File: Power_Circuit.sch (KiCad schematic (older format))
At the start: 33 parts, among them U1 B_Plug_5mm, U10 DSN2596, U11 B_Plug_5mm, U12 B_Plug_5mm, U13 B_Plug_5mm, U2 DSN2596, U3 DSN2596, U4 B_Plug_5mm, U5 B_Plug_5mm, U6 B_Plug_5mm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

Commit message: Nouvelle avancee, manque la protection reverse polarity
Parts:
- removed C1: CP, symbol Device:CP
- removed D1: LED, symbol Device:LED
- removed D2: D, symbol Device:D
- removed F1: Fuse, symbol Device:Fuse
- removed R1: R, symbol Device:R
- added BZ1: Buzzer, Buzzer_Beeper:Buzzer_12x9.5RM7.6, symbol Device:Buzzer
- added J1: Conn_01x09, symbol Connector_Generic:Conn_01x09
- added J2: Conn_01x04, symbol Connector_Generic:Conn_01x04
- added SW1: SW_Push, symbol Switch:SW_Push
- D3, D4, D5, D6, D7: footprint (none) -> LIB_BE_PHELMA_CMS:LED_1206_3216Metric_Pad1.42x1.75mm_HandSolder
- R2, R3, R4, R5, R6: footprint (none) -> LIB_BE_PHELMA_CMS:R_1206_3216Metric_Pad1.42x1.75mm_HandSolder
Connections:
- wire segments 100 -> 114
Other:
- note added: "Battery balance connector"
- note added: "Battery bipper buzzer"
- note added: "Battery bipper slot"
- note added: "Bipper\n"
- note added: "Reset if battery went too low"
- note removed: "Add a slot for a battery bipper"
- moved on the sheet: U1

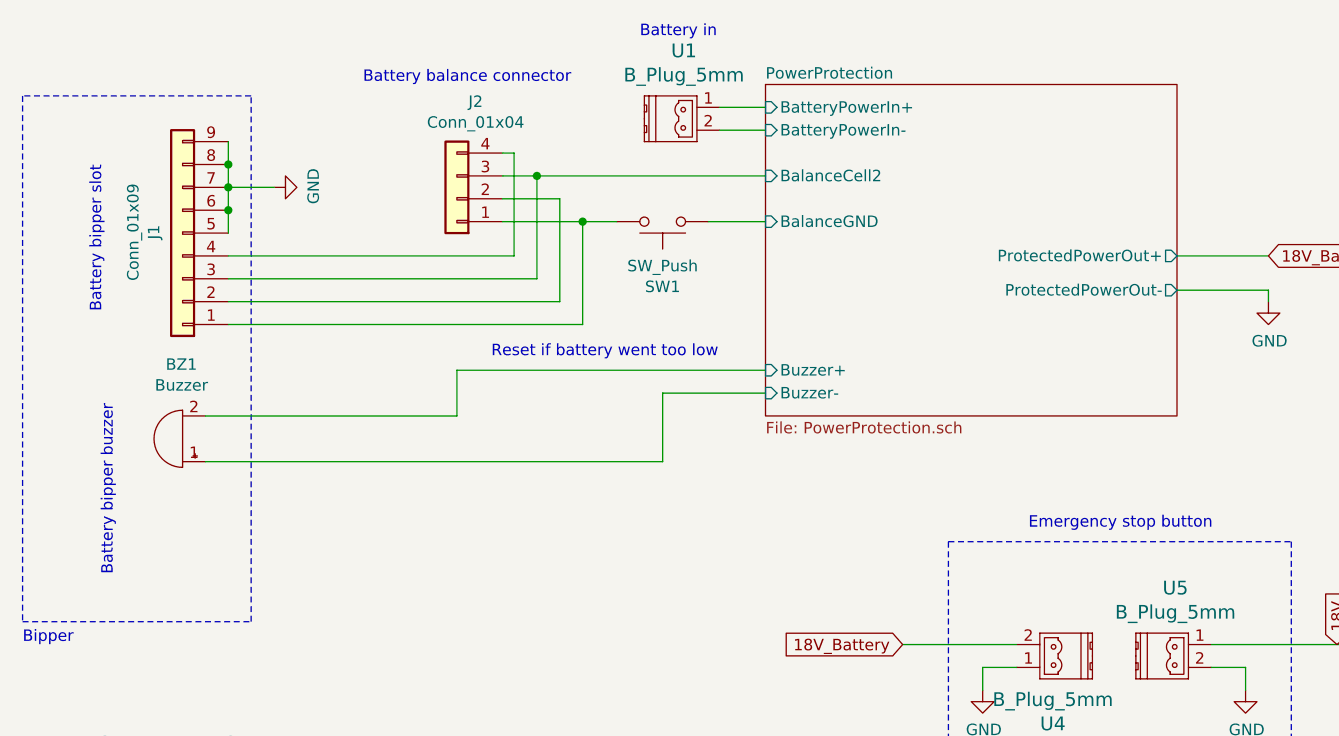
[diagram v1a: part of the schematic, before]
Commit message: Il reste a trouver empreintes et router
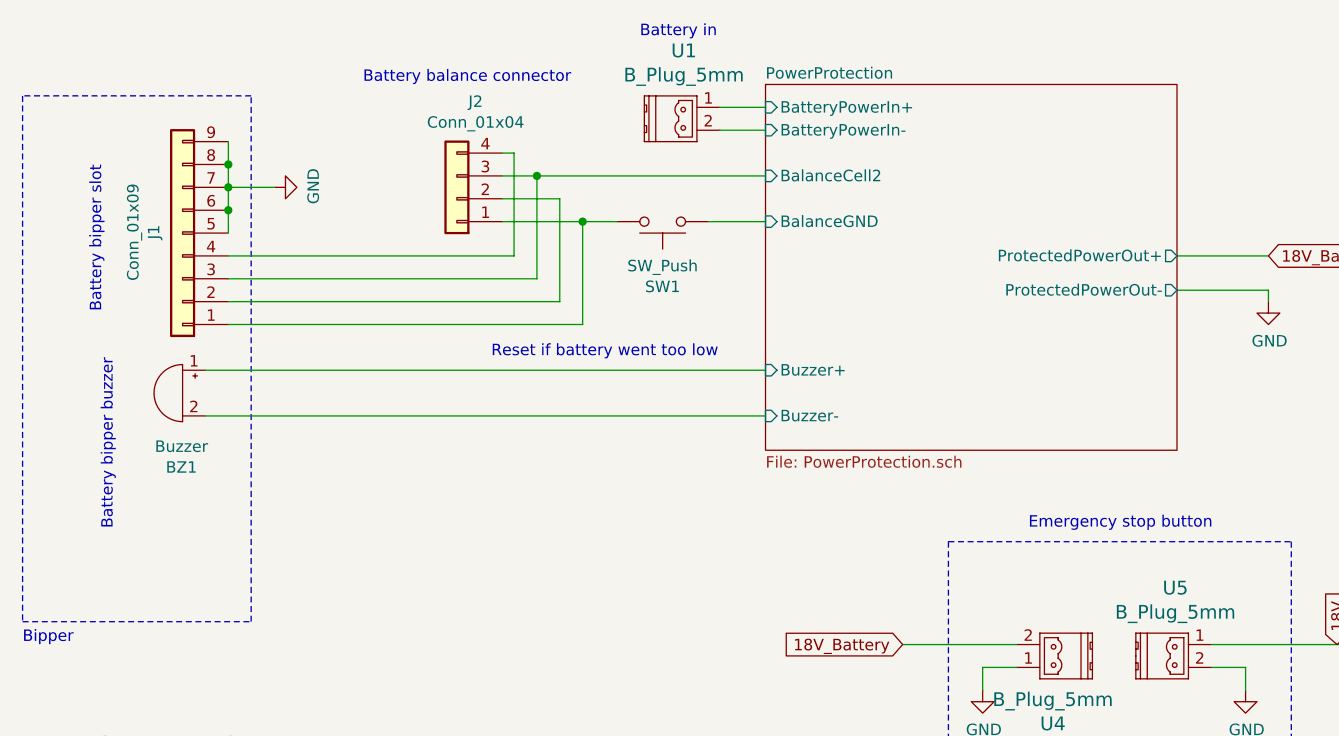
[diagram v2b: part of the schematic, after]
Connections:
- net PowerProtection/Buzzer+: now also BZ1.1 (-); no longer BZ1.2 (+)
- net PowerProtection/Buzzer-: now also BZ1.2 (+); no longer BZ1.1 (-)
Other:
- moved on the sheet: BZ1
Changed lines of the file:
@@
 $Descr A4 11693 8268
 encoding utf-8
-Sheet 1 3
+Sheet 1 2
 Title ""
 Date ""
@@
 Connection ~ 3350 5500
 $Sheet
-S 4250 1050 1800 1450
+S 4250 1050 1800 1600
 U 5F802FB9
 F0 "PowerProtection" 50
@@
 F7 "BalanceCell2" I L 4250 1450 50
 F8 "Buzzer+" I L 4250 2300 50
-F9 "Buzzer-" I L 4250 2400 50
+F9 "Buzzer-" I L 4250 2500 50
 $EndSheet
 Wire Wire Line
@@
 Wire Wire Line
 	3100 1550 3350 1550
-Text Notes 1400 3200 1    50   ~ 0
+Text Notes 1400 3000 1    50   ~ 0
 Battery bipper buzzer
 $Comp
 L Device:Buzzer BZ1
 U 1 1 5F94563A
-P 1700 2600
-F 0 "BZ1" H 1705 2275 50  0000 C CNN
-F 1 "Buzzer" H 1705 2366 50  0000 C CNN
-F 2 "Buzzer_Beeper:Buzzer_12x9.5RM7.6" V 1675 2700 50  0001 C CNN
-F 3 "~" V 1675 2700 50  0001 C CNN
-	1    1700 2600
-	-1   0    0    1
+P 1700 2400
+F 0 "BZ1" H 1705 2075 50  0000 C CNN
+F 1 "Buzzer" H 1705 2166 50  0000 C CNN
+F 2 "Buzzer_Beeper:Buzzer_12x9.5RM7.6" V 1675 2500 50  0001 C CNN
+F 3 "~" V 1675 2500 50  0001 C CNN
+	1    1700 2400
+	-1   0    0    -1
 $EndComp
 Wire Wire Line
@@
 Wire Wire Line
 	3450 1650 3100 1650
-Wire Wire Line
-	4250 2300 2900 2300
-Wire Wire Line
-	2900 2300 2900 2500
-Wire Wire Line
-	2900 2500 1800 2500
 Wire Wire Line
 	1900 1300 1900 1400
@@
 	-1   0    0    1
 $EndComp
-Wire Wire Line
-	3800 2700 3800 2400
-Wire Wire Line
-	3800 2400 4250 2400
 Text Notes 3050 2250 0    50   ~ 0
 Reset if battery went too low
@@
 Connection ~ 3450 1650
 Wire Wire Line
-	1800 2700 3800 2700
-Wire Wire Line
 	10200 3000 10250 3000
 Wire Wire Line
@@
 Wire Wire Line
 	1750 4100 1750 4200
+Wire Wire Line
+	1800 2300 4250 2300
+Wire Wire Line
+	1800 2500 4250 2500
 $EndSCHEMATC

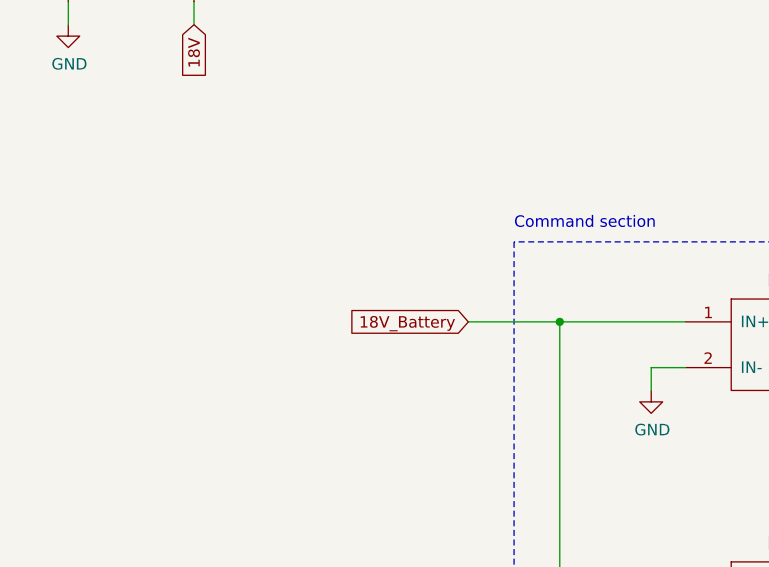
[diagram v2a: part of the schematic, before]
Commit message: ajout de la tirette
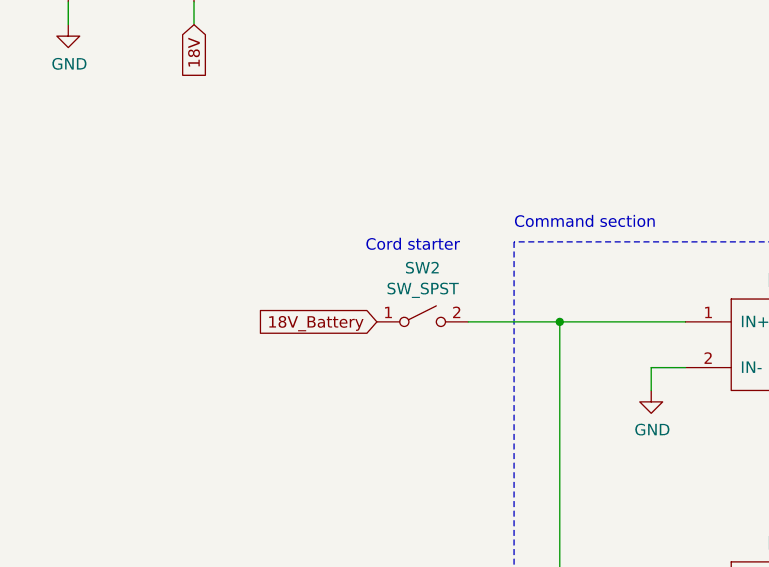
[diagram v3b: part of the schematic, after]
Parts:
- added SW2: SW_SPST, symbol Switch:SW_SPST
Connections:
- net 18V_Battery: now also SW2.1 (A); no longer U2.1 (IN+), U3.1 (IN+)
- new net: SW2.2 (B), U2.1 (IN+), U3.1 (IN+)
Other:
- note added: "Cord starter"
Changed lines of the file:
@@
 encoding utf-8
 Sheet 1 2
-Title ""
+Title "Power Circuit"
 Date ""
 Rev ""
-Comp ""
+Comp "Robotronik"
 Comment1 ""
 Comment2 ""
@@
 Text GLabel 4850 3500 0    50   Input ~ 0
 18V_Battery
-Text GLabel 2950 5500 0    50   Input ~ 0
+Text GLabel 2550 5500 0    50   Input ~ 0
 18V_Battery
 Wire Wire Line
@@
 Wire Wire Line
 	1800 2500 4250 2500
+$Comp
+L Switch:SW_SPST SW2
+U 1 1 5F8A3132
+P 2750 5500
+F 0 "SW2" H 2750 5735 50  0000 C CNN
+F 1 "SW_SPST" H 2750 5644 50  0000 C CNN
+F 2 "" H 2750 5500 50  0001 C CNN
+F 3 "~" H 2750 5500 50  0001 C CNN
+	1    2750 5500
+	1    0    0    -1
+$EndComp
+Text Notes 2500 5200 0    50   ~ 0
+Cord starter
 $EndSCHEMATC

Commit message: Fin du schema et routage
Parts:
- added BZ2: Buzzer, Buzzer_Beeper:Buzzer_12x9.5RM7.6, symbol Device:Buzzer
- F2, F3, F4, F5, F6: footprint (none) -> Fuse:Fuse_1210_3225Metric_Pad1.42x2.65mm_HandSolder
- J1: footprint (none) -> Connector_PinSocket_2.54mm:PinSocket_1x09_P2.54mm_Horizontal
- J2: footprint (none) -> Connector_PinHeader_2.54mm:PinHeader_1x04_P2.54mm_Vertical
- SW1: footprint (none) -> LIB_BE_PHELMA:R_Axial_DIN0207_L6.3mm_D2.5mm_P10.16mm_Horizontal
- SW2: value SW_SPST -> SW_STARTER; footprint (none) -> LIB_BE_PHELMA:R_Axial_DIN0207_L6.3mm_D2.5mm_P10.16mm_Horizontal
- U1: value B_Plug_5mm -> B_Plug_Battery_In; footprint (none) -> Connector_Phoenix_MC:PhoenixContact_MCV_1,5_2-G-3.81_1x02_P3.81mm_Vertical
- U10, U2, U3, U8, U9: footprint (none) -> DC_DC_LM2596_small:DC_DC_LM2596_small
- U11: value B_Plug_5mm -> B_Plug_12v_Motor1; footprint (none) -> Connector_Phoenix_MC:PhoenixContact_MCV_1,5_2-G-3.81_1x02_P3.81mm_Vertical
- U12: value B_Plug_5mm -> B_Plug_12v_Motor2; footprint (none) -> Connector_Phoenix_MC:PhoenixContact_MCV_1,5_2-G-3.81_1x02_P3.81mm_Vertical
- U13: value B_Plug_5mm -> B_Plug_5v_Actuator; footprint (none) -> Connector_Phoenix_MC:PhoenixContact_MCV_1,5_2-G-3.81_1x02_P3.81mm_Vertical
- U4: value B_Plug_5mm -> B_Plug_E-Stop_In; footprint (none) -> Connector_Phoenix_MC:PhoenixContact_MCV_1,5_2-G-3.81_1x02_P3.81mm_Vertical
- U5: value B_Plug_5mm -> B_Plug_E-Stop_out; footprint (none) -> Connector_Phoenix_MC:PhoenixContact_MCV_1,5_2-G-3.81_1x02_P3.81mm_Vertical
- U6: value B_Plug_5mm -> B_Plug_5V_Command; footprint (none) -> Connector_Phoenix_MC:PhoenixContact_MCV_1,5_2-G-3.81_1x02_P3.81mm_Vertical
- U7: value B_Plug_5mm -> B_Plug_7v5_Command; footprint (none) -> Connector_Phoenix_MC:PhoenixContact_MCV_1,5_2-G-3.81_1x02_P3.81mm_Vertical
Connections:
- net 18V: now also U5.2; no longer U5.1
- net GND: now also U5.1, BZ2.1 (-), BZ2.2 (+); no longer U5.2
- net PowerProtection/BatteryPowerIn+: now also U1.2; no longer U1.1
- net PowerProtection/BatteryPowerIn-: now also U1.1; no longer U1.2
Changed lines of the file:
@@
 F 0 "U8" H 8500 3587 60  0000 C CNN
 F 1 "DSN2596" H 8500 3481 60  0000 C CNN
-F 2 "" H 8500 3200 60  0001 C CNN
+F 2 "DC_DC_LM2596_small:DC_DC_LM2596_small" H 8500 3200 60  0001 C CNN
 F 3 "" H 8500 3200 60  0000 C CNN
 	1    8500 3200
@@
 F 0 "F4" H 9460 3146 50  0000 L CNN
 F 1 "Fuse" H 9460 3055 50  0000 L CNN
-F 2 "" V 9330 3100 50  0001 C CNN
+F 2 "Fuse:Fuse_1210_3225Metric_Pad1.42x2.65mm_HandSolder" V 9330 3100 50  0001 C CNN
 F 3 "~" H 9400 3100 50  0001 C CNN
 	1    9400 3100
@@
 P 3950 1200
 F 0 "U1" H 3893 1497 60  0000 C CNN
-F 1 "B_Plug_5mm" H 3893 1391 60  0000 C CNN
-F 2 "" H 3950 1200 60  0001 C CNN
+F 1 "B_Plug_Battery_In" H 3893 1391 60  0000 C CNN
+F 2 "Connector_Phoenix_MC:PhoenixContact_MCV_1,5_2-G-3.81_1x02_P3.81mm_Vertical" H 3950 1200 60  0001 C CNN
 F 3 "" H 3950 1200 60  0000 C CNN
 	1    3950 1200
-	1    0    0    -1
+	1    0    0    1
 $EndComp
 $Comp
@@
 P 10500 3150
 F 0 "U11" H 10443 3447 60  0000 C CNN
-F 1 "B_Plug_5mm" H 10443 3341 60  0000 C CNN
-F 2 "" H 10500 3150 60  0001 C CNN
+F 1 "B_Plug_12v_Motor1" H 10443 3341 60  0000 C CNN
+F 2 "Connector_Phoenix_MC:PhoenixContact_MCV_1,5_2-G-3.81_1x02_P3.81mm_Vertical" H 10500 3150 60  0001 C CNN
 F 3 "" H 10500 3150 60  0000 C CNN
 	1    10500 3150
@@
 F 0 "U9" H 8500 4687 60  0000 C CNN
 F 1 "DSN2596" H 8500 4581 60  0000 C CNN
-F 2 "" H 8500 4300 60  0001 C CNN
+F 2 "DC_DC_LM2596_small:DC_DC_LM2596_small" H 8500 4300 60  0001 C CNN
 F 3 "" H 8500 4300 60  0000 C CNN
 	1    8500 4300
@@
 F 0 "F5" H 9460 4246 50  0000 L CNN
 F 1 "Fuse" H 9460 4155 50  0000 L CNN
-F 2 "" V 9330 4200 50  0001 C CNN
+F 2 "Fuse:Fuse_1210_3225Metric_Pad1.42x2.65mm_HandSolder" V 9330 4200 50  0001 C CNN
 F 3 "~" H 9400 4200 50  0001 C CNN
 	1    9400 4200
@@
 P 10500 4250
 F 0 "U12" H 10443 4547 60  0000 C CNN
-F 1 "B_Plug_5mm" H 10443 4441 60  0000 C CNN
-F 2 "" H 10500 4250 60  0001 C CNN
+F 1 "B_Plug_12v_Motor2" H 10443 4441 60  0000 C CNN
+F 2 "Connector_Phoenix_MC:PhoenixContact_MCV_1,5_2-G-3.81_1x02_P3.81mm_Vertical" H 10500 4250 60  0001 C CNN
 F 3 "" H 10500 4250 60  0000 C CNN
 	1    10500 4250
@@
 F 0 "U10" H 8500 5787 60  0000 C CNN
 F 1 "DSN2596" H 8500 5681 60  0000 C CNN
-F 2 "" H 8500 5400 60  0001 C CNN
+F 2 "DC_DC_LM2596_small:DC_DC_LM2596_small" H 8500 5400 60  0001 C CNN
 F 3 "" H 8500 5400 60  0000 C CNN
 	1    8500 5400
@@
 F 0 "F6" H 9460 5346 50  0000 L CNN
 F 1 "Fuse" H 9460 5255 50  0000 L CNN
-F 2 "" V 9330 5300 50  0001 C CNN
+F 2 "Fuse:Fuse_1210_3225Metric_Pad1.42x2.65mm_HandSolder" V 9330 5300 50  0001 C CNN
 F 3 "~" H 9400 5300 50  0001 C CNN
 	1    9400 5300
@@
 P 10500 5350
 F 0 "U13" H 10443 5647 60  0000 C CNN
-F 1 "B_Plug_5mm" H 10443 5541 60  0000 C CNN
-F 2 "" H 10500 5350 60  0001 C CNN
+F 1 "B_Plug_5v_Actuator" H 10443 5541 60  0000 C CNN
+F 2 "Connector_Phoenix_MC:PhoenixContact_MCV_1,5_2-G-3.81_1x02_P3.81mm_Vertical" H 10500 5350 60  0001 C CNN
 F 3 "" H 10500 5350 60  0000 C CNN
 	1    10500 5350
@@
 F 0 "U2" H 4450 5987 60  0000 C CNN
 F 1 "DSN2596" H 4450 5881 60  0000 C CNN
-F 2 "" H 4450 5600 60  0001 C CNN
+F 2 "DC_DC_LM2596_small:DC_DC_LM2596_small" H 4450 5600 60  0001 C CNN
 F 3 "https://www.ti.com/lit/ds/symlink/lm2596.pdf" H 4450 5600 60  0001 C CNN
 	1    4450 5600
@@
 F 0 "F2" H 5410 5546 50  0000 L CNN
 F 1 "Fuse" H 5410 5455 50  0000 L CNN
-F 2 "" V 5280 5500 50  0001 C CNN
+F 2 "Fuse:Fuse_1210_3225Metric_Pad1.42x2.65mm_HandSolder" V 5280 5500 50  0001 C CNN
 F 3 "~" H 5350 5500 50  0001 C CNN
 	1    5350 5500
@@
 P 6450 5550
 F 0 "U6" H 6393 5847 60  0000 C CNN
-F 1 "B_Plug_5mm" H 6393 5741 60  0000 C CNN
-F 2 "" H 6450 5550 60  0001 C CNN
+F 1 "B_Plug_5V_Command" H 6393 5741 60  0000 C CNN
+F 2 "Connector_Phoenix_MC:PhoenixContact_MCV_1,5_2-G-3.81_1x02_P3.81mm_Vertical" H 6450 5550 60  0001 C CNN
 F 3 "" H 6450 5550 60  0000 C CNN
 	1    6450 5550
@@
 F 0 "U3" H 4450 7137 60  0000 C CNN
 F 1 "DSN2596" H 4450 7031 60  0000 C CNN
-F 2 "" H 4450 6750 60  0001 C CNN
+F 2 "DC_DC_LM2596_small:DC_DC_LM2596_small" H 4450 6750 60  0001 C CNN
 F 3 "" H 4450 6750 60  0000 C CNN
 	1    4450 6750
@@
 F 0 "F3" H 5410 6696 50  0000 L CNN
 F 1 "Fuse" H 5410 6605 50  0000 L CNN
-F 2 "" V 5280 6650 50  0001 C CNN
+F 2 "Fuse:Fuse_1210_3225Metric_Pad1.42x2.65mm_HandSolder" V 5280 6650 50  0001 C CNN
 F 3 "~" H 5350 6650 50  0001 C CNN
 	1    5350 6650
@@
 P 6450 6700
 F 0 "U7" H 6393 6997 60  0000 C CNN
-F 1 "B_Plug_5mm" H 6393 6891 60  0000 C CNN
-F 2 "" H 6450 6700 60  0001 C CNN
+F 1 "B_Plug_7v5_Command" H 6393 6891 60  0000 C CNN
+F 2 "Connector_Phoenix_MC:PhoenixContact_MCV_1,5_2-G-3.81_1x02_P3.81mm_Vertical" H 6450 6700 60  0001 C CNN
 F 3 "" H 6450 6700 60  0000 C CNN
 	1    6450 6700
@@
 P 5450 3550
 F 0 "U4" H 5393 3847 60  0000 C CNN
-F 1 "B_Plug_5mm" H 5393 3741 60  0000 C CNN
-F 2 "" H 5450 3550 60  0001 C CNN
+F 1 "B_Plug_E-Stop_In" H 5393 3741 60  0000 C CNN
+F 2 "Connector_Phoenix_MC:PhoenixContact_MCV_1,5_2-G-3.81_1x02_P3.81mm_Vertical" H 5450 3550 60  0001 C CNN
 F 3 "" H 5450 3550 60  0000 C CNN
 	1    5450 3550
@@
 P 6100 3550
 F 0 "U5" H 6043 3847 60  0000 C CNN
-F 1 "B_Plug_5mm" H 6043 3741 60  0000 C CNN
-F 2 "" H 6100 3550 60  0001 C CNN
+F 1 "B_Plug_E-Stop_out" H 6043 3741 60  0000 C CNN
+F 2 "Connector_Phoenix_MC:PhoenixContact_MCV_1,5_2-G-3.81_1x02_P3.81mm_Vertical" H 6100 3550 60  0001 C CNN
 F 3 "" H 6100 3550 60  0000 C CNN
 	1    6100 3550
-	1    0    0    -1
+	1    0    0    1
 $EndComp
 Wire Wire Line
@@
 F 0 "J1" V 1825 1696 50  0000 C CNN
 F 1 "Conn_01x09" V 1916 1696 50  0000 C CNN
-F 2 "" H 1700 1700 50  0001 C CNN
+F 2 "Connector_PinSocket_2.54mm:PinSocket_1x09_P2.54mm_Horizontal" H 1700 1700 50  0001 C CNN
 F 3 "~" H 1700 1700 50  0001 C CNN
 	1    1700 1700
@@
 F 0 "J2" H 2818 1125 50  0000 C CNN
 F 1 "Conn_01x04" H 2818 1216 50  0000 C CNN
-F 2 "" H 2900 1550 50  0001 C CNN
+F 2 "Connector_PinHeader_2.54mm:PinHeader_1x04_P2.54mm_Vertical" H 2900 1550 50  0001 C CNN
 F 3 "~" H 2900 1550 50  0001 C CNN
 	1    2900 1550
@@
 F 0 "SW1" H 3800 1935 50  0000 C CNN
 F 1 "SW_Push" H 3800 1844 50  0000 C CNN
-F 2 "" H 3800 1850 50  0001 C CNN
+F 2 "LIB_BE_PHELMA:R_Axial_DIN0207_L6.3mm_D2.5mm_P10.16mm_Horizontal" H 3800 1850 50  0001 C CNN
 F 3 "~" H 3800 1850 50  0001 C CNN
 	1    3800 1650
@@
 P 2750 5500
 F 0 "SW2" H 2750 5735 50  0000 C CNN
-F 1 "SW_SPST" H 2750 5644 50  0000 C CNN
-F 2 "" H 2750 5500 50  0001 C CNN
+F 1 "SW_STARTER" H 2750 5644 50  0000 C CNN
+F 2 "LIB_BE_PHELMA:R_Axial_DIN0207_L6.3mm_D2.5mm_P10.16mm_Horizontal" H 2750 5500 50  0001 C CNN
 F 3 "~" H 2750 5500 50  0001 C CNN
 	1    2750 5500
@@
 Text Notes 2500 5200 0    50   ~ 0
 Cord starter
+$Comp
+L Device:Buzzer BZ2
+U 1 1 5FB3C6D2
+P 1750 2950
+F 0 "BZ2" H 1755 2625 50  0000 C CNN
+F 1 "Buzzer" H 1755 2716 50  0000 C CNN
+F 2 "Buzzer_Beeper:Buzzer_12x9.5RM7.6" V 1725 3050 50  0001 C CNN
+F 3 "~" V 1725 3050 50  0001 C CNN
+	1    1750 2950
+	-1   0    0    -1
+$EndComp
+$Comp
+L power:GND #PWR0102
+U 1 1 5FB60BCF
+P 2050 2850
+F 0 "#PWR0102" H 2050 2600 50  0001 C CNN
+F 1 "GND" H 2055 2677 50  0000 C CNN
+F 2 "" H 2050 2850 50  0001 C CNN
+F 3 "" H 2050 2850 50  0001 C CNN
+	1    2050 2850
+	0    -1   -1   0
+$EndComp
+Wire Wire Line
+	2050 2850 1850 2850
+$Comp
+L power:GND #PWR0103
+U 1 1 5FB650C4
+P 2050 3050
+F 0 "#PWR0103" H 2050 2800 50  0001 C CNN
+F 1 "GND" H 2055 2877 50  0000 C CNN
+F 2 "" H 2050 3050 50  0001 C CNN
+F 3 "" H 2050 3050 50  0001 C CNN
+	1    2050 3050
+	0    -1   -1   0
+$EndComp
+Wire Wire Line
+	2050 3050 1850 3050
 $EndSCHEMATC

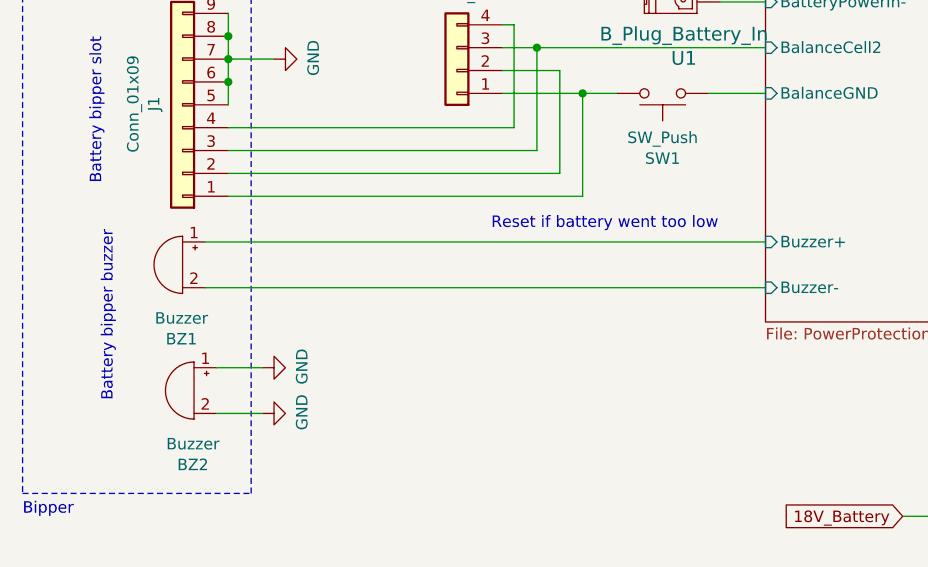
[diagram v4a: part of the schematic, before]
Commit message: Changement pour ajouter la possibiliter de court circuiter les 2 buzzers ou 1
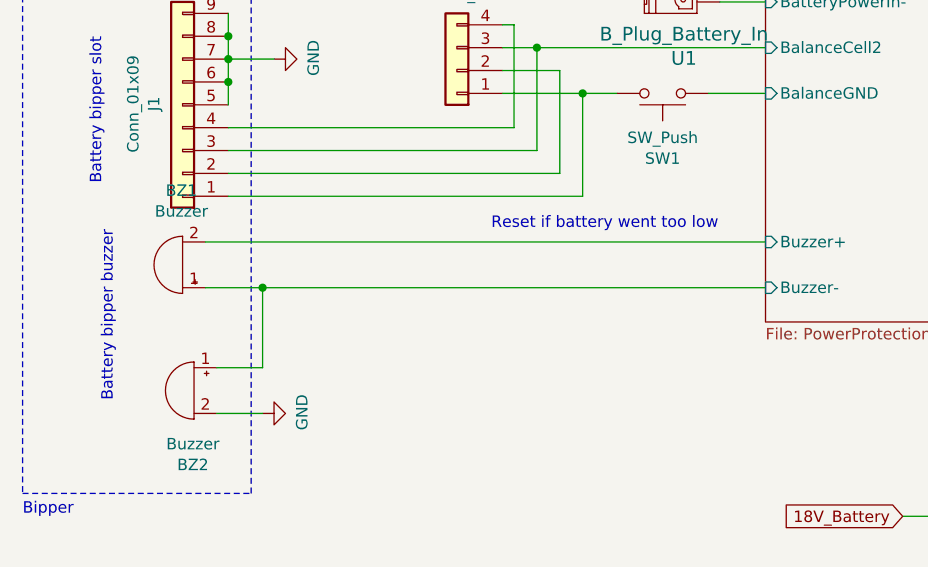
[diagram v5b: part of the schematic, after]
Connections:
- net GND: no longer BZ2.1 (-)
- net PowerProtection/Buzzer+: now also BZ1.2 (+); no longer BZ1.1 (-)
- net PowerProtection/Buzzer-: now also BZ1.1 (-), BZ2.1 (-); no longer BZ1.2 (+)
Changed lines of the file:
@@
 F 3 "~" V 1675 2500 50  0001 C CNN
 	1    1700 2400
-	-1   0    0    -1
+	-1   0    0    1
 $EndComp
 Wire Wire Line
@@
 	1800 2300 4250 2300
 Wire Wire Line
-	1800 2500 4250 2500
+	1800 2500 2050 2500
 $Comp
 L Switch:SW_SPST SW2
@@
 	-1   0    0    -1
 $EndComp
-$Comp
-L power:GND #PWR0102
-U 1 1 5FB60BCF
-P 2050 2850
-F 0 "#PWR0102" H 2050 2600 50  0001 C CNN
-F 1 "GND" H 2055 2677 50  0000 C CNN
-F 2 "" H 2050 2850 50  0001 C CNN
-F 3 "" H 2050 2850 50  0001 C CNN
-	1    2050 2850
-	0    -1   -1   0
-$EndComp
 Wire Wire Line
 	2050 2850 1850 2850
@@
 Wire Wire Line
 	2050 3050 1850 3050
+Wire Wire Line
+	2050 2850 2050 2500
+Connection ~ 2050 2500
+Wire Wire Line
+	2050 2500 4250 2500
 $EndSCHEMATC
